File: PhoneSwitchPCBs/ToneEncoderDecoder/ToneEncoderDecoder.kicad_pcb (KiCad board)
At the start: 2 copper layers, 100 x 100 mm, 124 parts, among them IC1 XRA1203IG24TR-F, IC2 NXB0108PWJ, IC3 74HC4316, IC4 74HC4316, IC5 TL074*DT, IC6 TL074*DT, IC7 TL072, IC8 MT8870DN1, IC9 MT8870DN1, J1 Tone Bus, J2 Power + Control, Q1 XP231N02013R-G, Q2 XP231N02013R-G, Y1 3.579545 MHz

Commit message: More work on PCB Layout
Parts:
- moved R24 236.8 mm to (39.7, 64.6)
- moved R22 226.2 mm to (39.0, 53.0)
- moved R19 219.5 mm to (69.0, 56.5), turned to -90 degrees
- moved R18 218.3 mm to (40.6, 58.3)
- moved R27 197.9 mm to (71.7, 57.5), turned to 180 degrees
- moved D3 194.3 mm to (77.0, 58.5)
- moved R1 138.5 mm to (71.7, 46.2)
- moved D1 136.7 mm to (77.0, 43.1)
- moved R3 53.1 mm to (77.0, 46.2), turned to 180 degrees
- moved C18 47.0 mm to (71.7, 48.7)
- moved C24 43.9 mm to (77.0, 52.9)
- moved C22 41.4 mm to (71.7, 52.9), turned to 0 degrees
- moved R32 40.9 mm to (240.0, 74.1)
- moved R7 37.3 mm to (77.0, 55.4), turned to 180 degrees
- moved R17 36.5 mm to (69.0, 45.1), turned to 90 degrees
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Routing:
- net Net-(C18-Pad2): track 0.00 -> 16.5 mm
- net Net-(C22-Pad2): track 0.00 -> 16.4 mm
- net Net-(D1-Pad1): track 0.00 -> 16.0 mm
- net Net-(D3-Pad1): track 0.00 -> 16.0 mm
- net Net-(C20-Pad1): track 0.00 -> 2.81 mm
- net Net-(C24-Pad1): track 0.00 -> 2.78 mm
- net Net-(D1-Pad3): track 0.00 -> 1.86 mm
- net Net-(D3-Pad3): track 0.00 -> 1.84 mm

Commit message: Mostly Finished Tone Gen Layout
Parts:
- moved R35 229.4 mm to (55.8, 31.5)
- moved R30 206.3 mm to (81.6, 36.0), turned to 180 degrees
- moved R28 170.4 mm to (109.1, 36.0)
- moved R20 169.3 mm to (111.9, 37.0), turned to 90 degrees
- moved R6 162.9 mm to (109.1, 38.0), turned to 180 degrees
- moved R32 160.2 mm to (81.6, 49.4), turned to 180 degrees
- moved R33 154.3 mm to (55.8, 53.3)
- moved R26 150.9 mm to (109.1, 49.4)
- moved R12 147.3 mm to (86.9, 38.0), turned to 180 degrees
- moved R8 147.2 mm to (103.8, 38.0)
- moved R4 143.1 mm to (103.8, 47.3)
- moved D10 142.7 mm to (86.9, 50.3)
- moved R40 141.1 mm to (86.9, 53.3), turned to 180 degrees
- moved R36 140.7 mm to (103.8, 31.5)
- moved R38 138.6 mm to (86.9, 31.5), turned to 180 degrees
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- renumbered D4 to De
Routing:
- net Net-(D4-Pad3): track 0.00 -> 23.6 mm, vias 0 -> 3
- net Net-(D2-Pad3): track 0.00 -> 23.2 mm, vias 0 -> 3
- net Net-(D1-Pad3): track 1.86 -> 24.9 mm, vias 0 -> 3
- net Net-(D10-Pad3): track 0.00 -> 22.9 mm, vias 0 -> 3
- net Net-(D3-Pad3): track 1.84 -> 24.4 mm, vias 0 -> 3
- net Net-(D6-Pad3): track 0.00 -> 22.3 mm, vias 0 -> 3
- net Net-(D4-Pad1): track 0.00 -> 16.2 mm
- net Net-(D6-Pad1): track 0.00 -> 16.0 mm
- net Net-(D2-Pad1): track 0.00 -> 15.8 mm
- net Net-(D10-Pad1): track 0.00 -> 15.6 mm
- net Net-(C19-Pad2): track 0.00 -> 14.0 mm
- net Net-(C23-Pad2): track 0.00 -> 13.9 mm
- net Net-(C31-Pad2): track 0.00 -> 13.8 mm
- net Net-(C27-Pad2): track 0.00 -> 13.7 mm
- net Net-(C21-Pad1): track 0.00 -> 2.81 mm
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
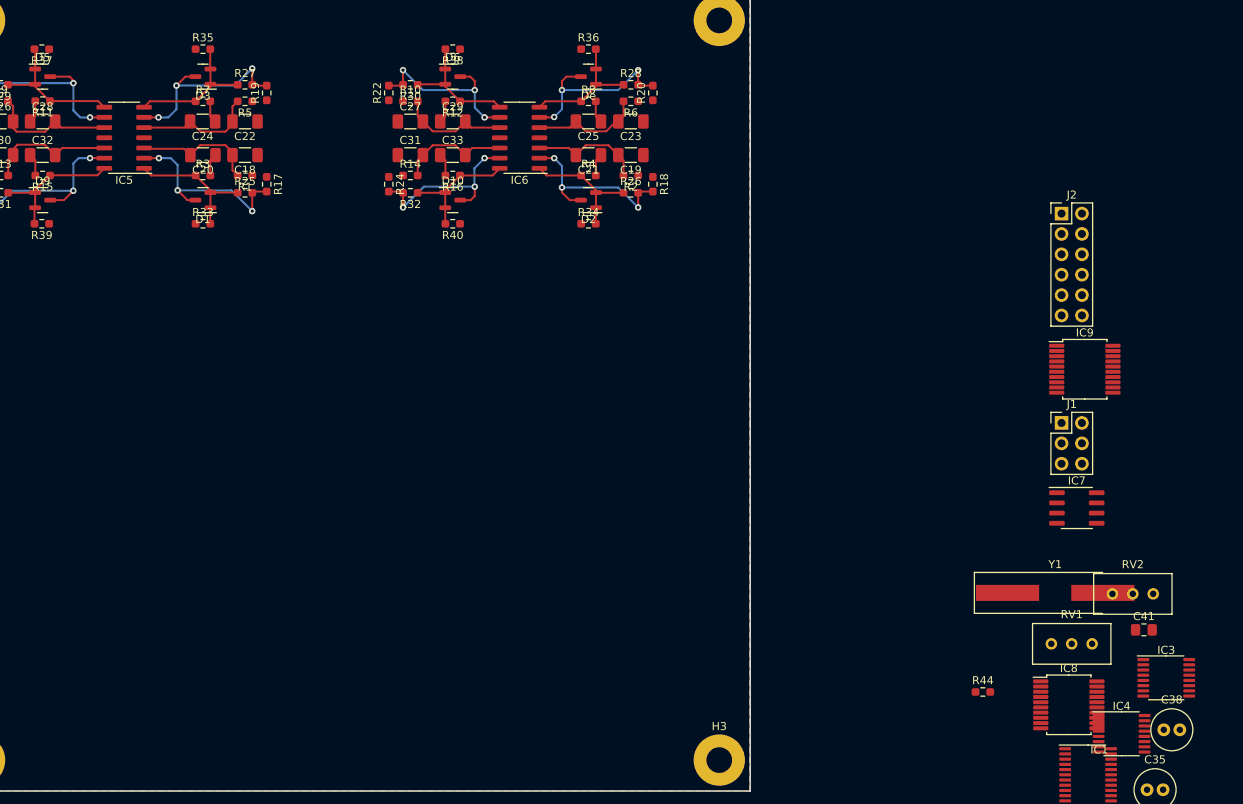
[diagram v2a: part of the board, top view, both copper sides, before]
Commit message: Connect signals to switch IC
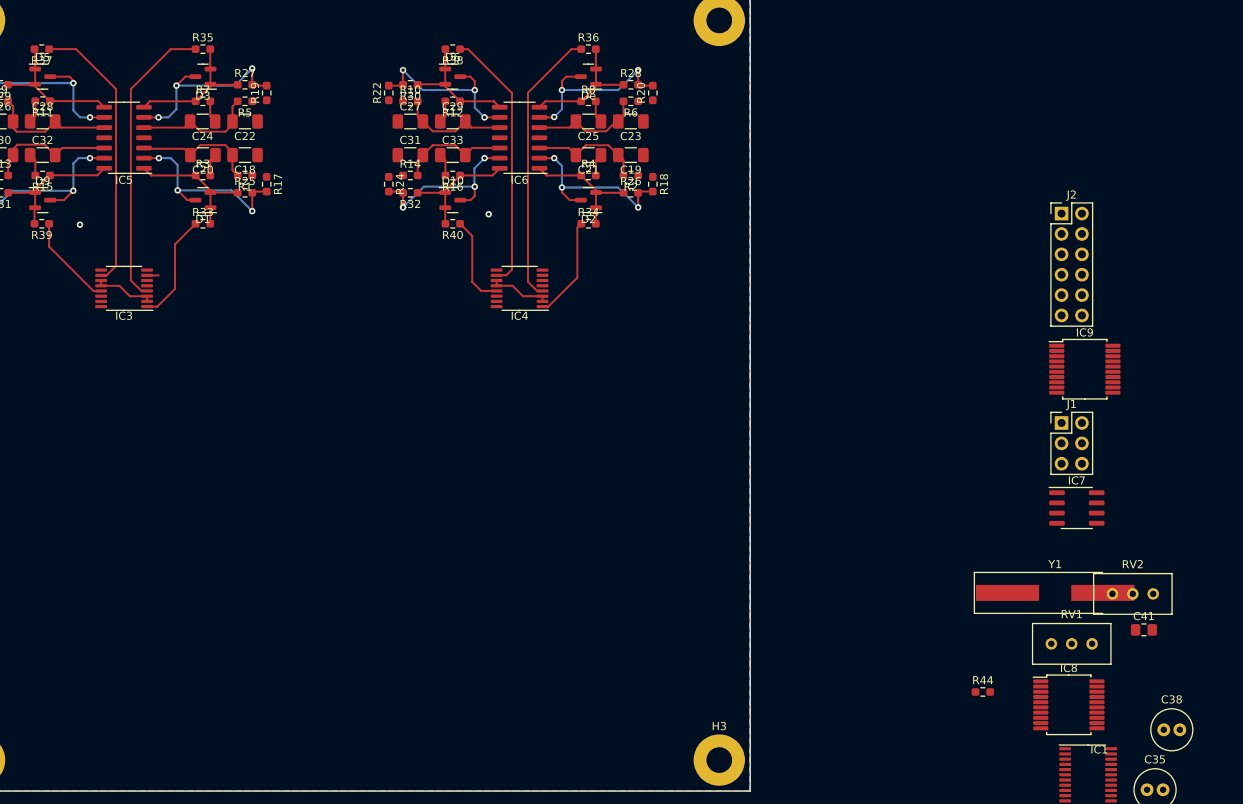
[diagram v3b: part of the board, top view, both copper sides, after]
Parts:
- moved IC3 138.7 mm to (45.9, 61.3), turned to 180 degrees
- moved IC4 93.3 mm to (95.2, 61.3), turned to 180 degrees
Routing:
- net Net-(IC3-Pad4): track 0.00 -> 36.5 mm
- net Net-(IC3-Pad10): track 0.00 -> 34.8 mm
- net Net-(IC4-Pad4): track 0.00 -> 34.7 mm
- net Net-(IC4-Pad10): track 0.00 -> 32.9 mm
- net Net-(IC3-Pad1): track 0.00 -> 13.6 mm
- net Net-(IC4-Pad1): track 0.00 -> 12.7 mm
- net Net-(IC3-Pad13): track 0.00 -> 11.6 mm
- net Net-(IC4-Pad13): track 0.00 -> 11.4 mm
- net Net-(IC3-Pad11): track 0.00 -> 7.56 mm
- net Net-(IC4-Pad11): track 0.00 -> 7.56 mm
- net GND: track 0.00 -> 1.46 mm, vias 0 -> 2

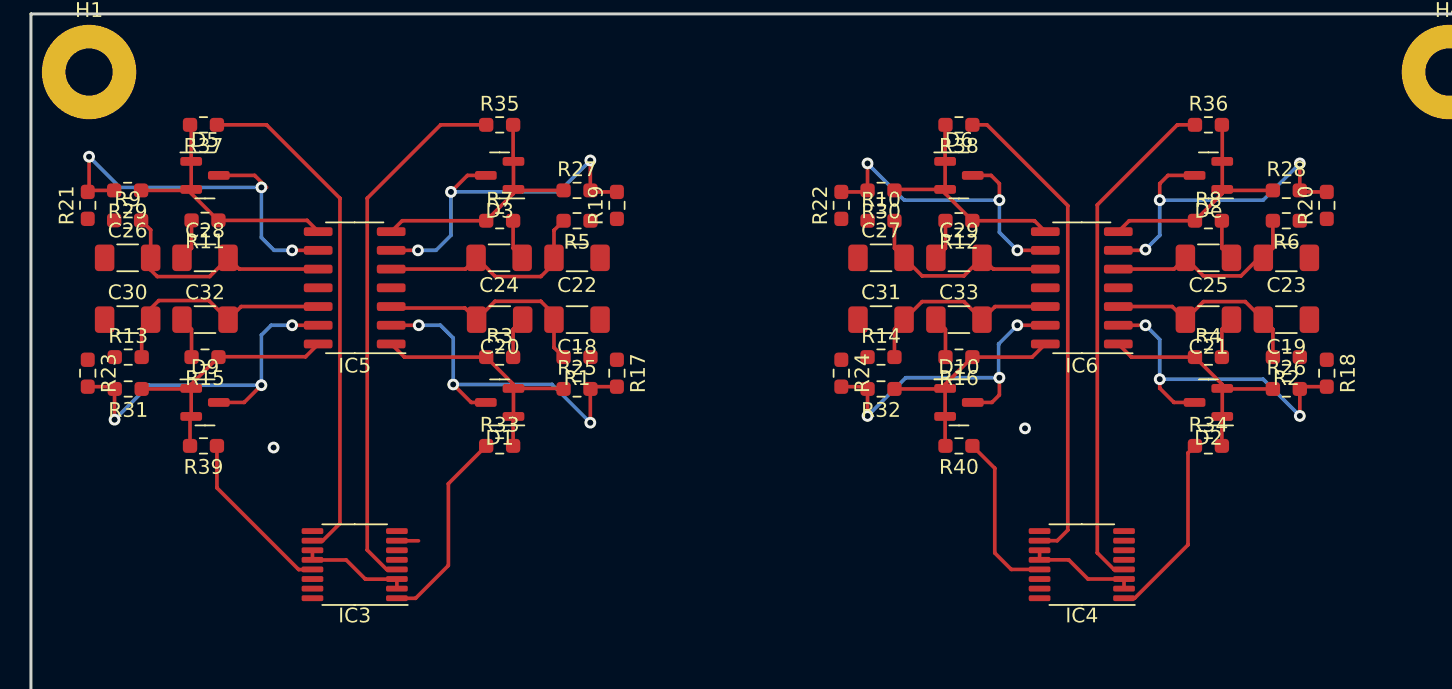
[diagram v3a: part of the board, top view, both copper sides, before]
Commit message: Cleaned up tone generator placement
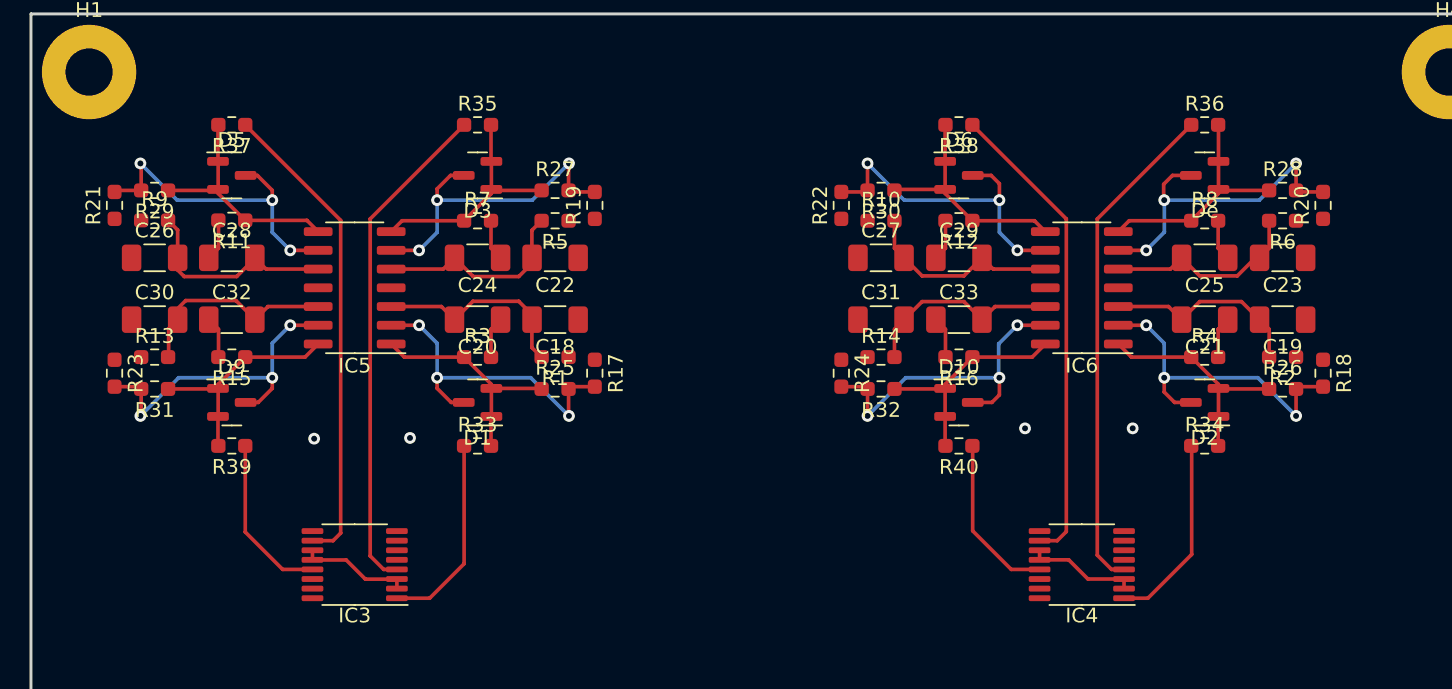
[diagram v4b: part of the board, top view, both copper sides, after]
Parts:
- moved R37 1.92 mm to (37.6, 31.5)
- moved R39 1.92 mm to (37.6, 53.3)
- moved C26 1.83 mm to (32.4, 40.5)
- moved C30 1.83 mm to (32.4, 44.7)
- moved R29 1.83 mm to (32.4, 36.0)
- moved R9 1.83 mm to (32.4, 38.0)
- moved R21 1.82 mm to (29.7, 37.0)
- moved C28 1.82 mm to (37.6, 40.5)
- moved C32 1.82 mm to (37.6, 44.7)
- moved D5 1.82 mm to (37.6, 35.0)
- moved D9 1.82 mm to (37.6, 50.3)
- moved R11 1.82 mm to (37.6, 38.0)
- moved R15 1.82 mm to (37.6, 47.3)
- moved R23 1.82 mm to (29.7, 48.4)
- moved R13 1.79 mm to (32.4, 47.3)
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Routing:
- net Net-(D5-Pad3): track 27.9 -> 22.3 mm
- net Net-(D9-Pad3): track 25.8 -> 22.7 mm
- net Net-(IC3-Pad4): track 36.5 -> 34.1 mm
- net Net-(D1-Pad3): track 24.9 -> 22.6 mm
- net Net-(IC3-Pad10): track 34.8 -> 32.5 mm
- net Net-(D3-Pad3): track 24.4 -> 22.4 mm
- net Net-(D5-Pad1): track 17.8 -> 16.0 mm
- net Net-(C26-Pad2): track 16.8 -> 15.0 mm
- net Net-(C30-Pad2): track 16.1 -> 14.2 mm
- net Net-(D9-Pad1): track 17.3 -> 15.6 mm
- net Net-(D3-Pad1): track 17.4 -> 16.0 mm
- net Net-(D1-Pad1): track 17.0 -> 15.5 mm
- net Net-(C22-Pad2): track 15.4 -> 13.9 mm
- net GND: track 1.46 -> 0.00 mm, vias 2 -> 4
- net Net-(C18-Pad2): track 15.4 -> 14.1 mm
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
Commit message: Redoing layout
Redoing layout to fix the issues related to the in/mm switch at some point and me not noticing.
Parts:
- removed De: PMBD7000, Package_TO_SOT_SMD:SOT-23
- added D4: PMBD7000, Package_TO_SOT_SMD:SOT-23, F.Cu at (228.9, 50.7)
- moved R22 175.3 mm to (254.1, 43.0), turned to 0 degrees
- moved R32 163.9 mm to (245.4, 43.0), turned to 0 degrees
- moved R30 161.7 mm to (242.2, 55.0), turned to 0 degrees
- moved IC3 156.3 mm to (202.1, 55.2), turned to 0 degrees
- moved R24 150.8 mm to (229.4, 58.6), turned to 0 degrees
- moved R40 145.5 mm to (232.0, 63.6), turned to 0 degrees
- moved R26 143.8 mm to (252.6, 45.5)
- moved D10 142.1 mm to (228.9, 55.1)
- moved R10 140.9 mm to (213.5, 87.8)
- moved R2 139.4 mm to (248.3, 48.0), turned to 0 degrees
- moved R12 138.9 mm to (219.5, 79.7), turned to 0 degrees
- moved R14 138.5 mm to (219.0, 65.5)
- moved R36 136.9 mm to (239.6, 47.5)
- moved R28 135.3 mm to (242.5, 57.5)
- moved R16 134.2 mm to (218.3, 74.7), turned to 0 degrees
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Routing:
- net Net-(IC3-Pad4): track 34.1 -> 0.00 mm
- net Net-(IC4-Pad4): track 34.0 -> 0.00 mm
- net Net-(IC3-Pad10): track 32.5 -> 0.00 mm
- net Net-(IC4-Pad10): track 32.3 -> 0.00 mm
- net Net-(D10-Pad3): track 22.9 -> 0.00 mm, vias 3 -> 0
- net Net-(D4-Pad3): track 22.7 -> 0.00 mm, vias 3 -> 0
- net Net-(D2-Pad3): track 22.6 -> 0.00 mm, vias 3 -> 0
- net Net-(D6-Pad3): track 22.3 -> 0.00 mm, vias 3 -> 0
- net Net-(D6-Pad1): track 16.0 -> 0.00 mm
- net Net-(D4-Pad1): track 16.0 -> 0.00 mm
- net Net-(D2-Pad1): track 15.6 -> 0.00 mm
- net Net-(D10-Pad1): track 15.6 -> 0.00 mm
- net Net-(C31-Pad2): track 13.8 -> 0.00 mm
- net Net-(C19-Pad2): track 13.8 -> 0.00 mm
- net Net-(C27-Pad2): track 13.7 -> 0.00 mm
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
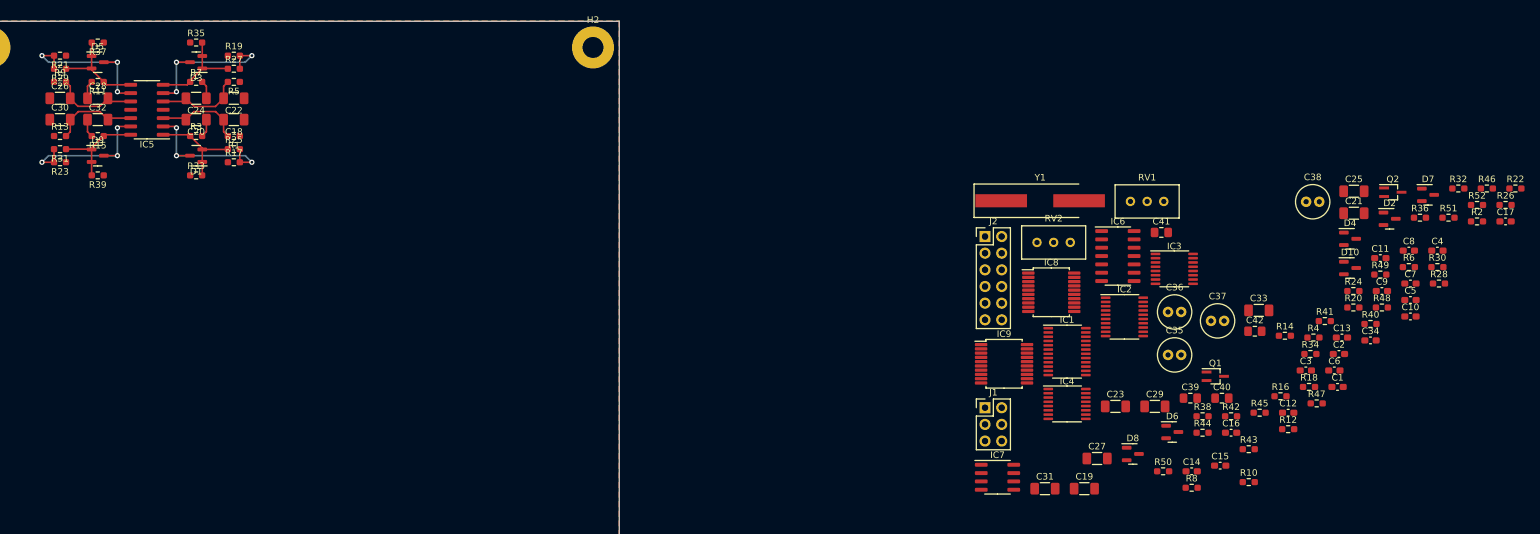
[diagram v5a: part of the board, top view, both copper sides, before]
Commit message: Laid out tone gens again
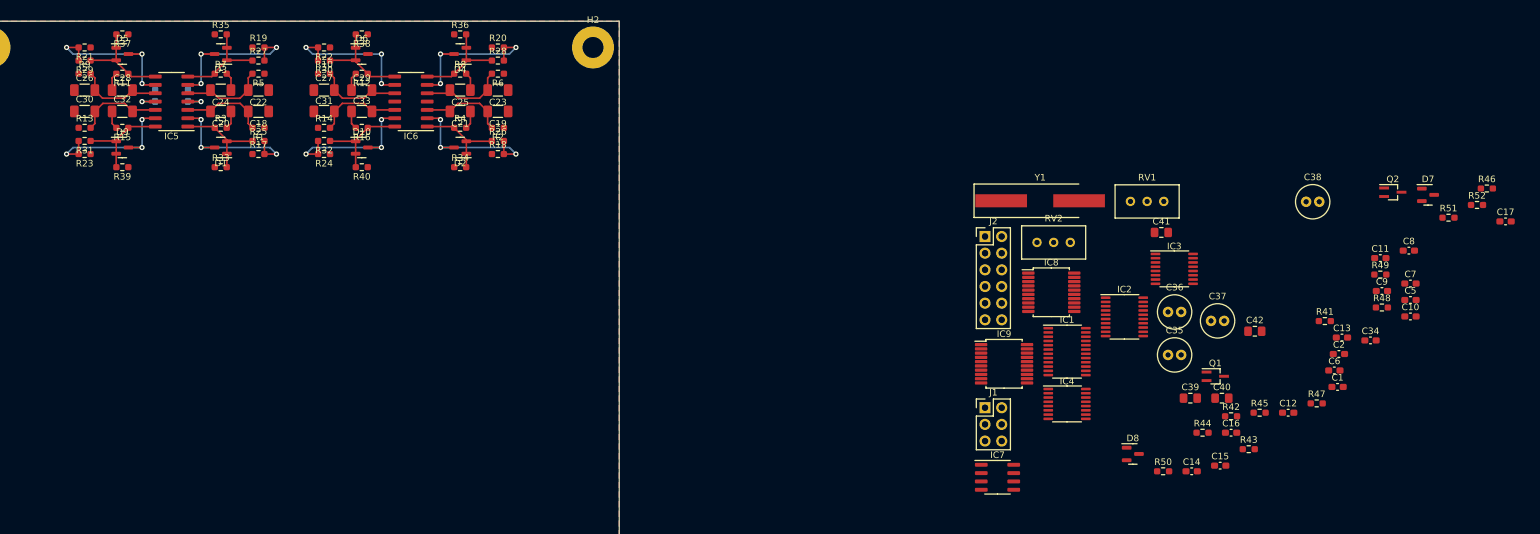
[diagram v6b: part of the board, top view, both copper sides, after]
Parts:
- C3, C4: moved to B.Cu
- moved C4 196.9 mm to (46.8, 28.9), turned to -90 degrees
- moved R22 182.9 mm to (72.5, 21.5), turned to 180 degrees
- moved C3 175.5 mm to (51.8, 28.9), turned to 90 degrees
- moved R32 173.1 mm to (72.5, 35.8), turned to 180 degrees
- moved R30 172.6 mm to (72.5, 23.5), turned to 180 degrees
- moved R24 158.3 mm to (72.5, 37.8), turned to 180 degrees
- moved R40 155.6 mm to (78.2, 39.8), turned to 180 degrees
- moved R10 154.1 mm to (72.5, 25.5)
- moved R26 153.9 mm to (99.0, 35.8)
- moved D10 151.8 mm to (78.2, 36.8)
- moved R12 151.3 mm to (78.2, 25.5), turned to 180 degrees
- moved R2 149.9 mm to (99.0, 33.8), turned to 180 degrees
- moved R14 149.9 mm to (72.5, 33.8)
- moved R36 149.0 mm to (93.2, 19.5)
- moved R28 147.4 mm to (99.0, 23.5)
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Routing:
- net Net-(D4-Pad3): track 0.00 -> 24.4 mm, vias 0 -> 3
- net Net-(D2-Pad3): track 0.00 -> 24.2 mm, vias 0 -> 3
- net Net-(D10-Pad3): track 0.00 -> 24.2 mm, vias 0 -> 3
- net Net-(D6-Pad3): track 0.00 -> 22.4 mm, vias 0 -> 3
- net Net-(D6-Pad1): track 0.00 -> 15.0 mm
- net Net-(D4-Pad1): track 0.00 -> 15.0 mm
- net Net-(D2-Pad1): track 0.00 -> 14.9 mm
- net Net-(D10-Pad1): track 0.00 -> 14.9 mm
- net Net-(C27-Pad2): track 0.00 -> 13.2 mm
- net Net-(C23-Pad2): track 0.00 -> 13.2 mm
- net Net-(C31-Pad2): track 0.00 -> 13.1 mm
- net Net-(C19-Pad2): track 0.00 -> 13.1 mm
- net -5VA: track 0.00 -> 4.04 mm, vias 0 -> 1
- net +5VA: track 0.00 -> 4.04 mm, vias 0 -> 1
- net Net-(C33-Pad1): track 0.00 -> 2.77 mm
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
